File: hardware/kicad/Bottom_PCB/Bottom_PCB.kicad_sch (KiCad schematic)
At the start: 38 parts, among them Q7 IAUC60N04S6N031H, Q8 IAUC60N04S6N031H, Q9 IAUC60N04S6N031H, U5 STSPIN32F0ATR

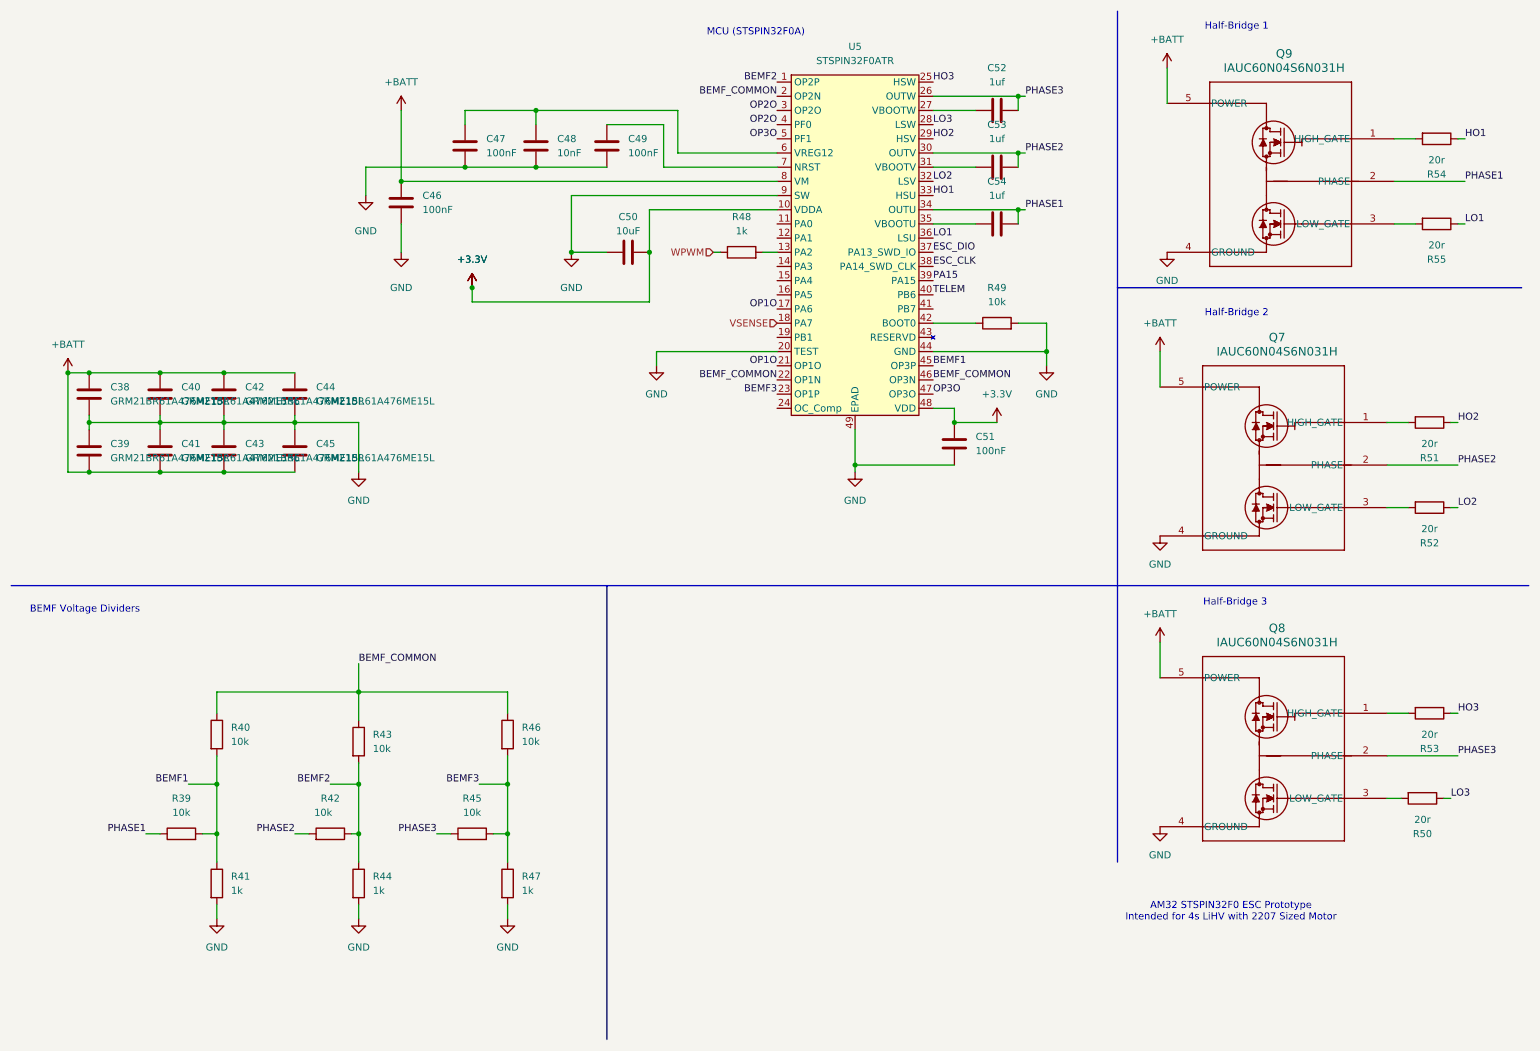
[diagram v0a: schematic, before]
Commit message: Bottom PCB Design Checked and should be ready for review
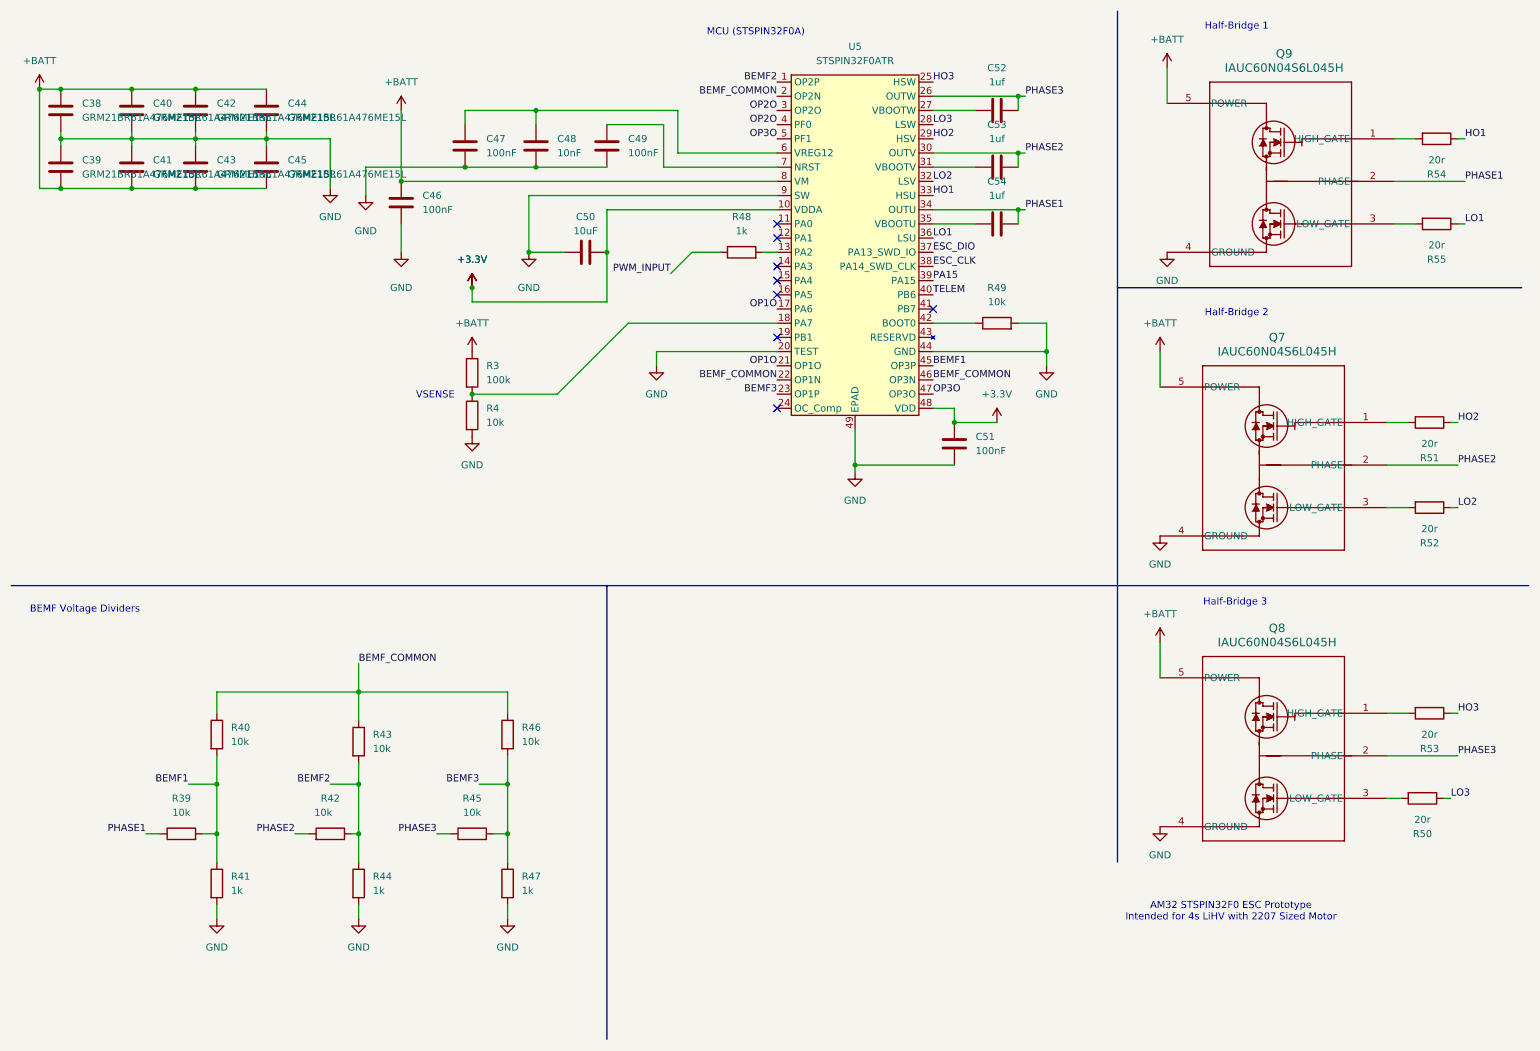
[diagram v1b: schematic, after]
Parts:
- added R3: 100k, Resistor_SMD:R_0402_1005Metric_Pad0.72x0.64mm_HandSolder, symbol Device:R
- added R4: 10k, Resistor_SMD:R_0402_1005Metric_Pad0.72x0.64mm_HandSolder, symbol Device:R
- Q7, Q8, Q9: value IAUC60N04S6N031H -> IAUC60N04S6L045H
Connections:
- net +BATT: now also R3.1
- net GND: now also R4.2
- net VSENSE: no longer names the net of U5.18 (PA7)
- net VSENSE: now also R3.2, R4.1
- net WPWM renamed PWM_INPUT
- no-connect marks 0 -> 8
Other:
- note added: "VSENSE"
- moved on the sheet: C50
